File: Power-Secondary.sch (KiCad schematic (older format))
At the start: 50 parts, among them J1 Primary Battery +12VDC, J10 BPS +12V, J2 PRIM BATT DISCNCT, J3 BPS MAIN SUPPLY, J4 JUMP START, J5 DashBoard HORN CTL, J6 DashBoard DRV FAN CTL, J7 HORN +12V, J8 DRIVER FAN +12V, J9 RADIOS +12V, K1 G5Q-1, K2 G5Q-1, K3 G5Q-1, SW1 Batt Check, SW2 BPS PWR CHECK, SW3 RADIO PWR CHECK

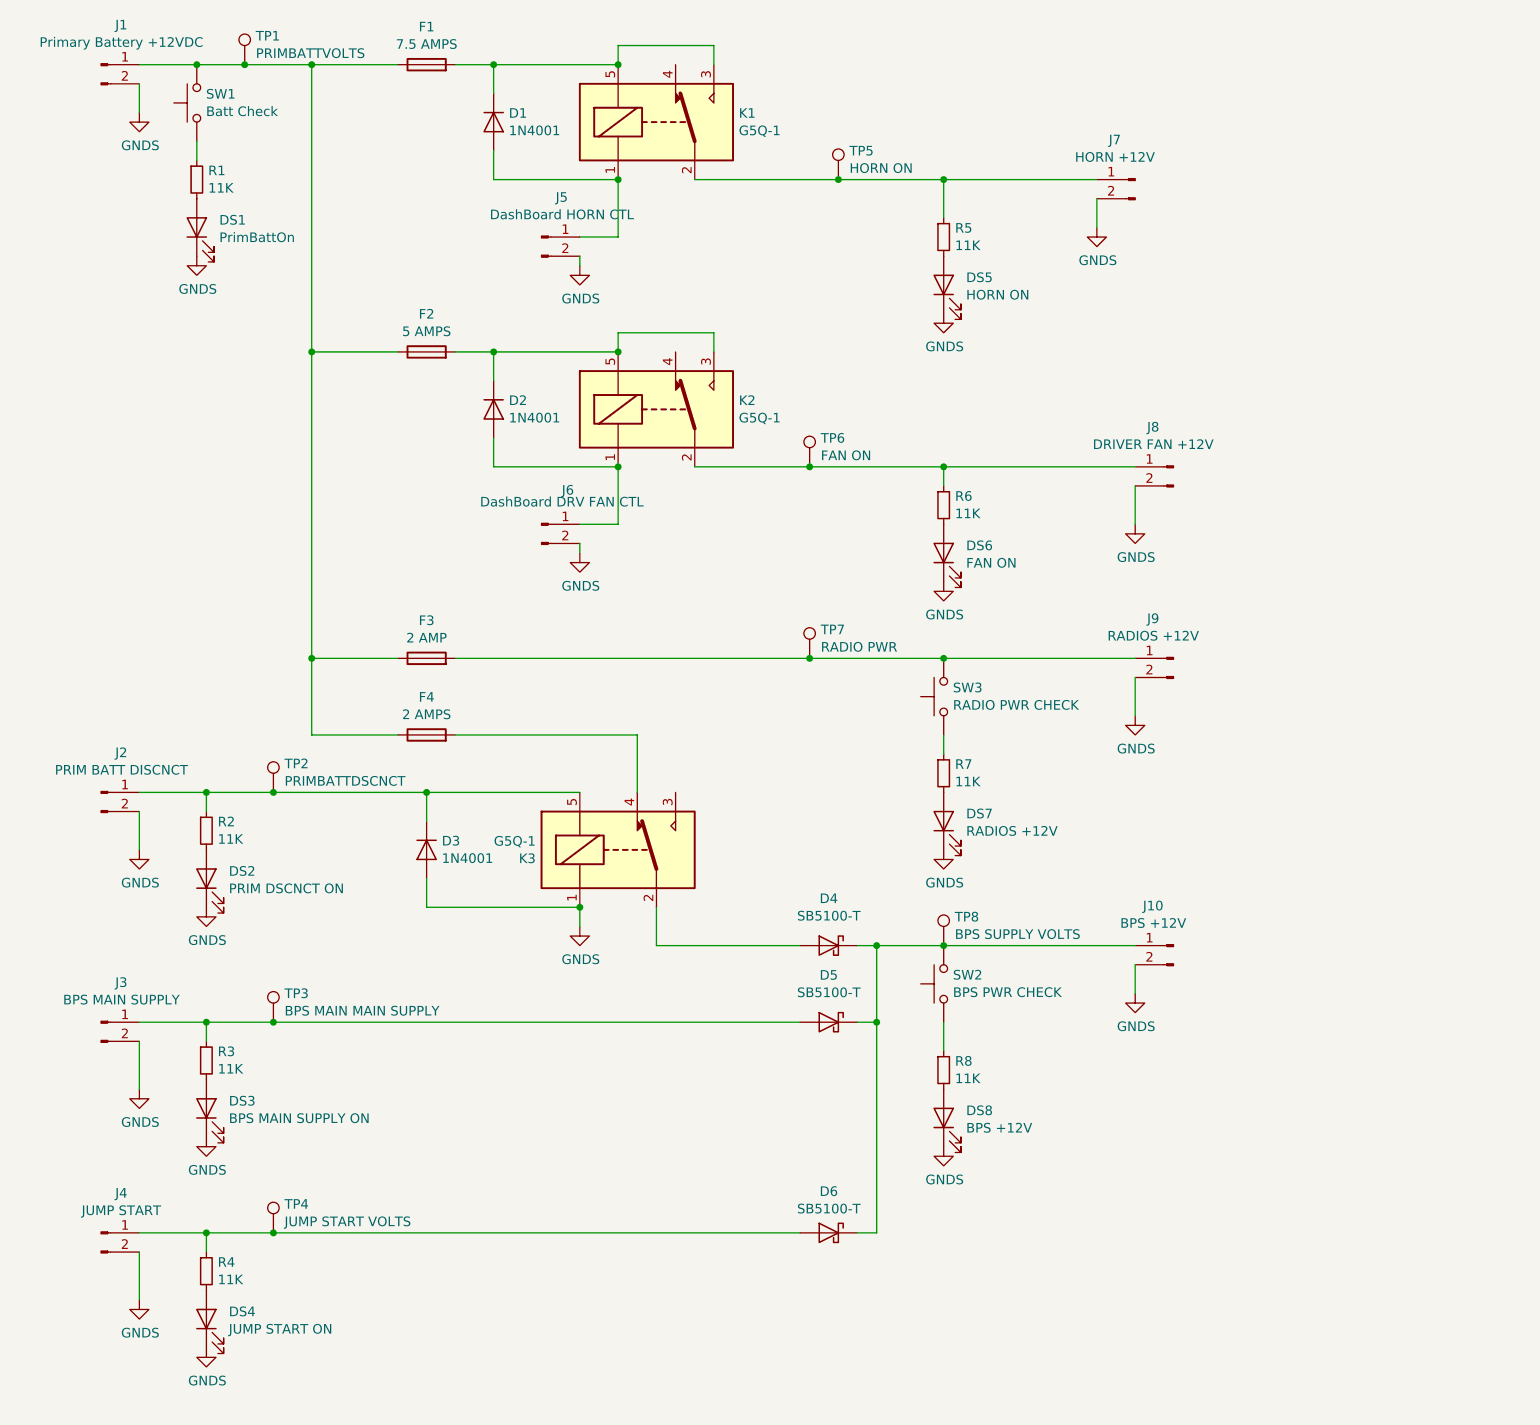
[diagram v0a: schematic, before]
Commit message: Secondary board v1.1 (#2)
* Updated PBB to better match Hannah's standards

* Adds power planes to secondary power board

* Updates schematics to match secondary power board v1.1

* Adds gitignore file

* Creates and deletes gerbers for release and finishes routing tracks

* Adds dimensions to PCB

Co-authored-by: Umar Burney <47867985+Emeraldness@users.noreply.github.com>
Co-authored-by: Sijin Woo <sijin.woo@utexas.edu>
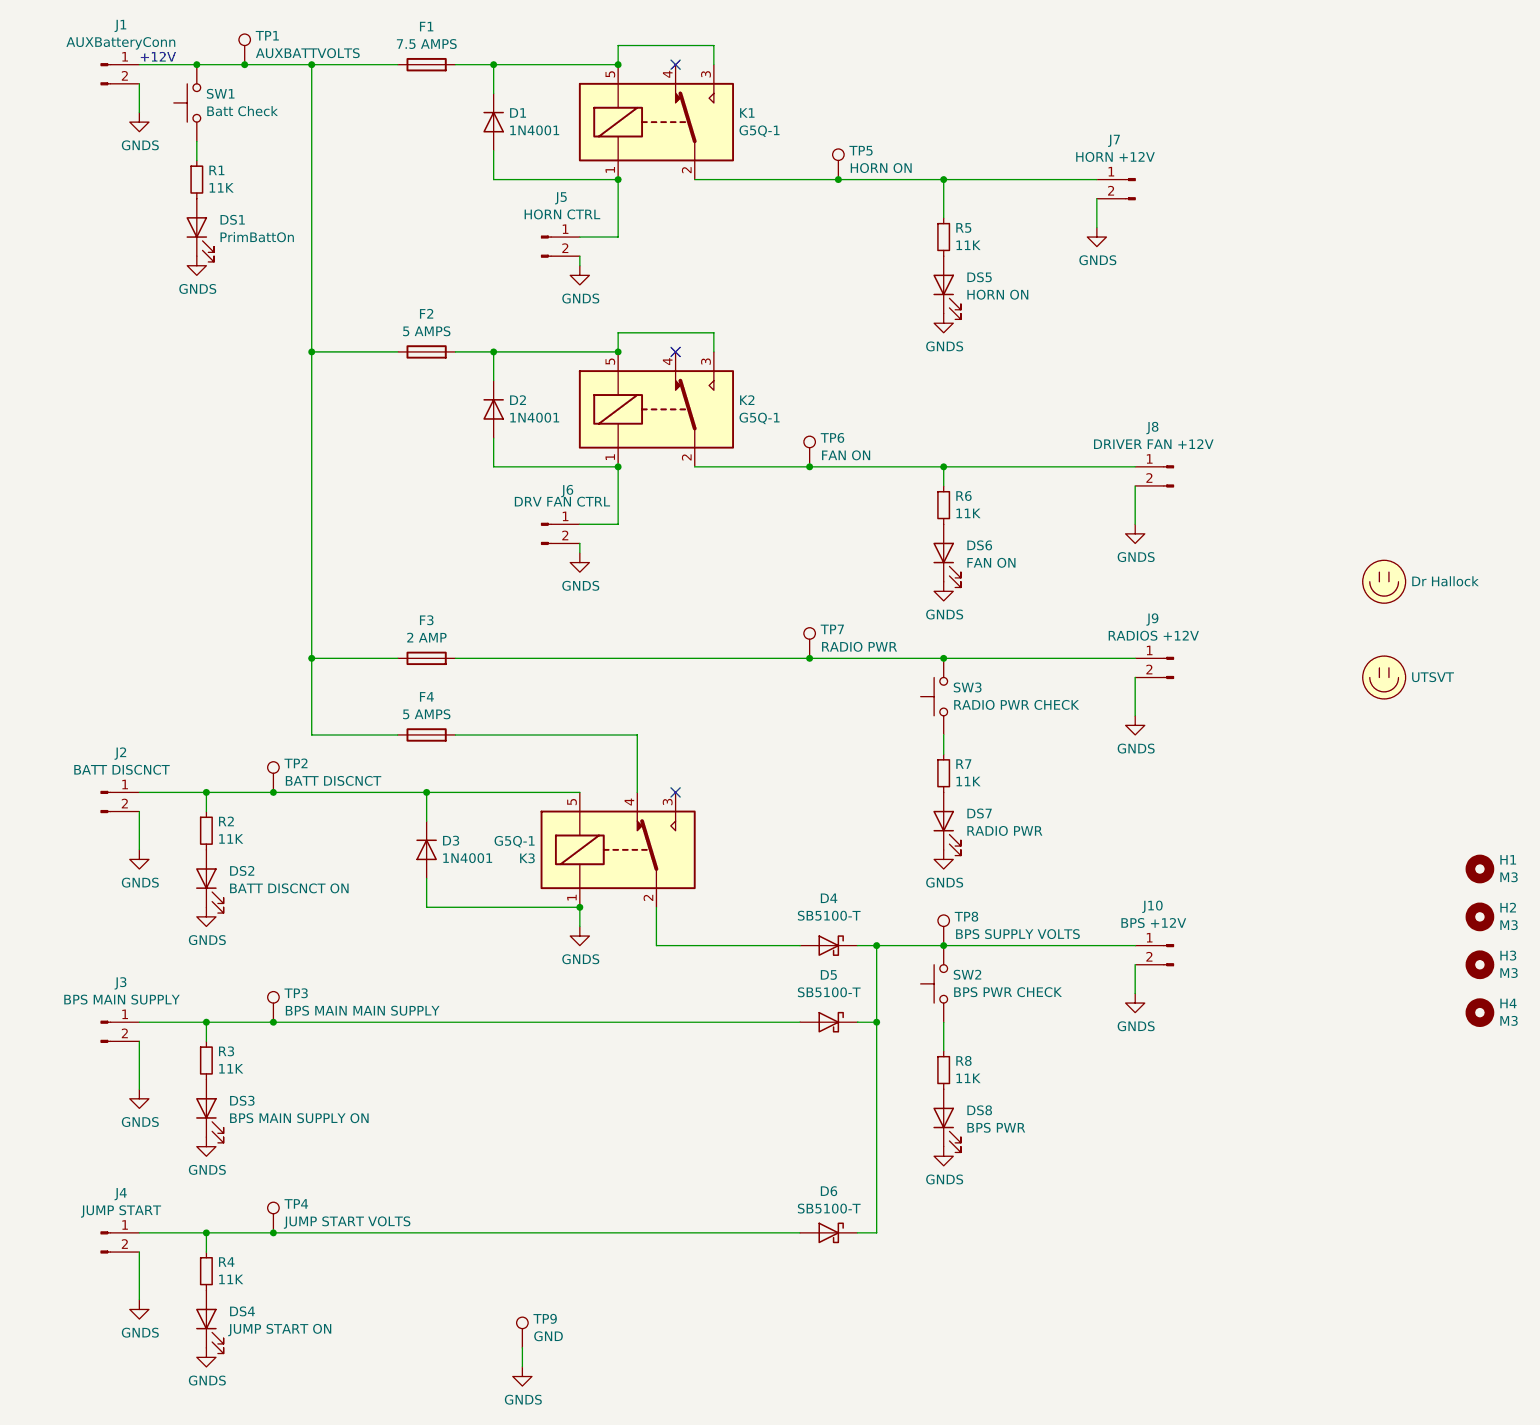
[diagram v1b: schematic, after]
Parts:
- added H1, H2, H3, H4: M3, MountingHole:MountingHole_3mm, symbol Mechanical:MountingHole
- added LOGO1: Dr Hallock, UTSVT_Special:Hallock_Image, symbol utsvt-misc:Logo_Placeholder
- added LOGO2: UTSVT, UTSVT_Special:UTSVT_Logo_Symbol, symbol utsvt-misc:Logo_Placeholder
- added TP9: GND, TestPoint:TestPoint_Pad_2.0x2.0mm, symbol Connector:TestPoint
- D1, D2, D3: footprint Diode_THT:D_DO-41_SOD81_P10.16mm_Horizontal -> Diode_THT:D_DO-15_P12.70mm_Horizontal
- D4, D5, D6: footprint Diode_THT:D_DO-201AD_P12.70mm_Horizontal -> Diode_THT:D_DO-201AD_P15.24mm_Horizontal
- DS2: value PRIM DSCNCT ON -> BATT DISCNCT ON
- DS7: value RADIOS +12V -> RADIO PWR
- DS8: value BPS +12V -> BPS PWR
- F4: value 2 AMPS -> 5 AMPS
- J1: value Primary Battery +12VDC -> AUXBatteryConn
- J2: value PRIM BATT DISCNCT -> BATT DISCNCT
- J5: value DashBoard HORN CTL -> HORN CTRL
- J6: value DashBoard DRV FAN CTL -> DRV FAN CTRL
- R1, R2, R3, R4, R5, R6, R7, R8: footprint Resistor_THT:R_Axial_DIN0204_L3.6mm_D1.6mm_P7.62mm_Horizontal -> Resistor_THT:R_Axial_DIN0207_L6.3mm_D2.5mm_P10.16mm_Horizontal
- TP1: value PRIMBATTVOLTS -> AUXBATTVOLTS
- TP2: value PRIMBATTDSCNCT -> BATT DISCNCT
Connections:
- net GNDS: now also TP9.1
- no-connect marks 0 -> 3
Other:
- note added: "+12V"

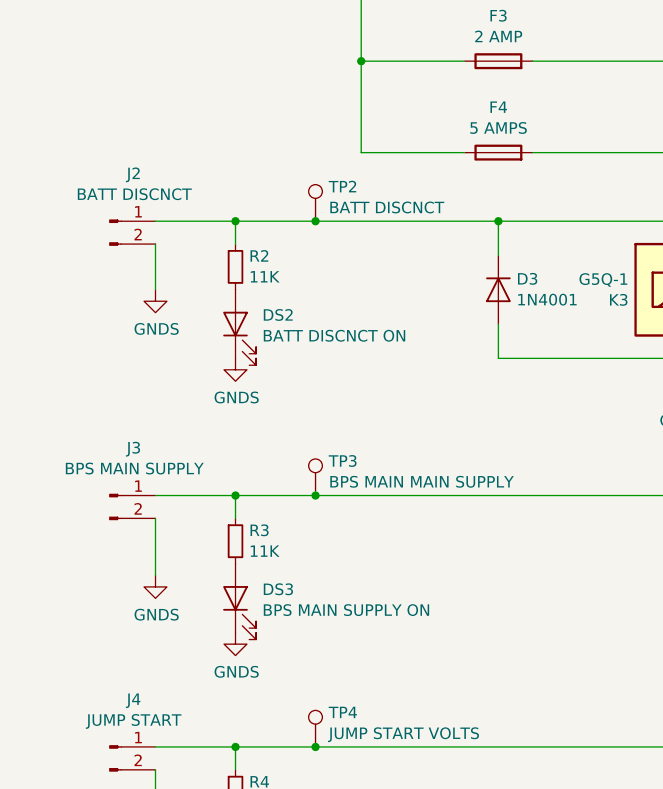
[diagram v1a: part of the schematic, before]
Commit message: Secondary Power Board CDR Edits (#3)
* Combines disconnect and main supply for BPS into one connector

* Rearranges labels and adds gerbers
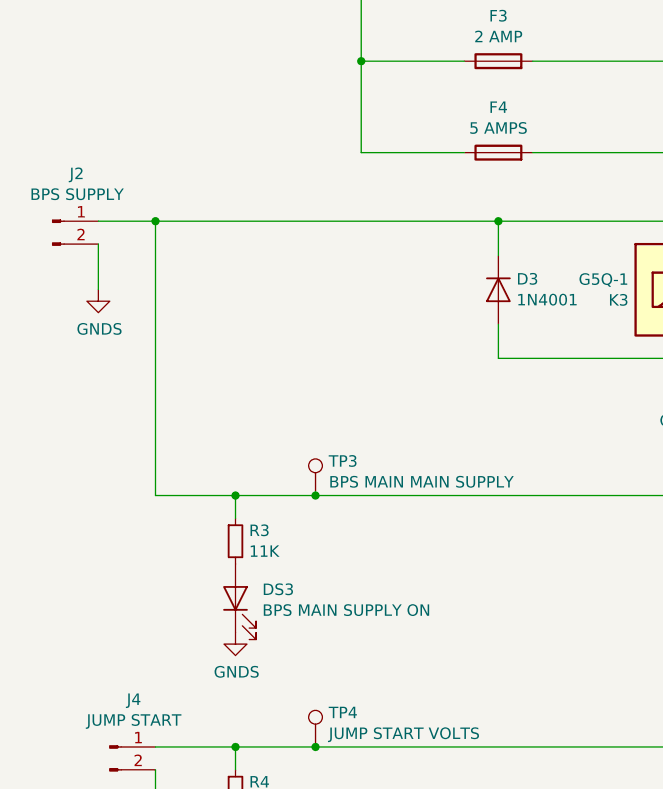
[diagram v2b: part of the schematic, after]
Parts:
- removed DS2: BATT DISCNCT ON, LED_THT:LED_D3.0mm, symbol Device:LED
- removed J3: BPS MAIN SUPPLY, Connector_Molex:Molex_Micro-Fit_3.0_43650-0215_1x02_P3.00mm_Vertical, symbol Connector:Conn_01x02_Male
- removed R2: 11K, Resistor_THT:R_Axial_DIN0207_L6.3mm_D2.5mm_P10.16mm_Horizontal, symbol Device:R_Small
- removed TP2: BATT DISCNCT, TestPoint:TestPoint_Pad_2.0x2.0mm, symbol Connector:TestPoint
- J2: value BATT DISCNCT -> BPS SUPPLY
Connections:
- net at D3.1 (K), J2.1 (Pin_1), K3.5: now also D5.2 (A), R3.1, TP3.1
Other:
- moved on the sheet: J2
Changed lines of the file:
@@
 L Connector:Conn_01x02_Male J2
 U 1 1 5BD1F5D8
-P 1800 4600
-F 0 "J2" H 1906 4778 50  0000 C BNN
-F 1 "BATT DISCNCT" H 1906 4687 50  0000 C BNN
-F 2 "Connector_Molex:Molex_Micro-Fit_3.0_43650-0215_1x02_P3.00mm_Vertical" H 1800 4600 50  0001 C CNN
-F 3 "~" H 1800 4600 50  0001 C CNN
-	1    1800 4600
+P 1550 4600
+F 0 "J2" H 1656 4778 50  0000 C BNN
+F 1 "BPS SUPPLY" H 1656 4687 50  0000 C BNN
+F 2 "Connector_Molex:Molex_Micro-Fit_3.0_43650-0215_1x02_P3.00mm_Vertical" H 1550 4600 50  0001 C CNN
+F 3 "~" H 1550 4600 50  0001 C CNN
+	1    1550 4600
 	1    0    0    -1
 $EndComp
@@
 L power:GNDS #PWR0109
 U 1 1 5BD2580C
-P 2000 4900
-F 0 "#PWR0109" H 2000 4650 50  0001 C CNN
-F 1 "GNDS" H 2005 4727 50  0000 C CNN
-F 2 "" H 2000 4900 50  0001 C CNN
-F 3 "" H 2000 4900 50  0001 C CNN
-	1    2000 4900
+P 1750 4900
+F 0 "#PWR0109" H 1750 4650 50  0001 C CNN
+F 1 "GNDS" H 1755 4727 50  0000 C CNN
+F 2 "" H 1750 4900 50  0001 C CNN
+F 3 "" H 1750 4900 50  0001 C CNN
+	1    1750 4900
 	1    0    0    -1
 $EndComp
@@
 $EndComp
 Wire Wire Line
-	2000 4600 2350 4600
-$Comp
-L power:GNDS #PWR0111
-U 1 1 5BD2B1A6
-P 2350 5200
-F 0 "#PWR0111" H 2350 4950 50  0001 C CNN
-F 1 "GNDS" H 2355 5027 50  0000 C CNN
-F 2 "" H 2350 5200 50  0001 C CNN
-F 3 "" H 2350 5200 50  0001 C CNN
-	1    2350 5200
-	1    0    0    -1
-$EndComp
-$Comp
-L Device:R_Small R2
-U 1 1 5BD2B1AC
-P 2350 4800
-F 0 "R2" H 2409 4846 50  0000 L CNN
-F 1 "11K" H 2409 4755 50  0000 L CNN
-F 2 "Resistor_THT:R_Axial_DIN0207_L6.3mm_D2.5mm_P10.16mm_Horizontal" H 2350 4800 50  0001 C CNN
-F 3 "~" H 2350 4800 50  0001 C CNN
-	1    2350 4800
-	1    0    0    -1
-$EndComp
-Wire Wire Line
-	2350 4700 2350 4600
-$Comp
-L Device:LED DS2
-U 1 1 5BD2B1B4
-P 2350 5050
-F 0 "DS2" V 2388 4933 50  0000 R CNN
-F 1 "BATT DISCNCT ON" V 2297 4933 50  0000 R CNN
-F 2 "LED_THT:LED_D3.0mm" H 2350 5050 50  0001 C CNN
-F 3 "~" H 2350 5050 50  0001 C CNN
-	1    2350 5050
-	0    -1   -1   0
-$EndComp
-Wire Wire Line
-	2000 4700 2000 4900
+	1750 4600 2000 4600
+Wire Wire Line
+	1750 4700 1750 4900
 $Comp
 L Device:Fuse F3
@@
 	0    -1   -1   0
 $EndComp
-Connection ~ 2350 4600
 Connection ~ 2900 800
 Wire Wire Line
@@
 Wire Wire Line
 	4600 4300 4600 4600
-Wire Wire Line
-	2350 4600 2700 4600
-$Comp
-L Connector:Conn_01x02_Male J3
-U 1 1 5BD7A592
-P 1800 5800
-F 0 "J3" H 1906 5978 50  0000 C BNN
-F 1 "BPS MAIN SUPPLY" H 1906 5887 50  0000 C BNN
-F 2 "Connector_Molex:Molex_Micro-Fit_3.0_43650-0215_1x02_P3.00mm_Vertical" H 1800 5800 50  0001 C CNN
-F 3 "~" H 1800 5800 50  0001 C CNN
-	1    1800 5800
-	1    0    0    -1
-$EndComp
-$Comp
-L power:GNDS #PWR0115
-U 1 1 5BD7A599
-P 2000 6150
-F 0 "#PWR0115" H 2000 5900 50  0001 C CNN
-F 1 "GNDS" H 2005 5977 50  0000 C CNN
-F 2 "" H 2000 6150 50  0001 C CNN
-F 3 "" H 2000 6150 50  0001 C CNN
-	1    2000 6150
-	1    0    0    -1
-$EndComp
-Wire Wire Line
-	2000 5900 2000 6150
-$Comp
-L power:GNDS #PWR0116
-U 1 1 5BD7A5A0
-P 2350 6400
-F 0 "#PWR0116" H 2350 6150 50  0001 C CNN
-F 1 "GNDS" H 2355 6227 50  0000 C CNN
-F 2 "" H 2350 6400 50  0001 C CNN
-F 3 "" H 2350 6400 50  0001 C CNN
-	1    2350 6400
-	1    0    0    -1
-$EndComp
-$Comp
-L Device:R_Small R3
-U 1 1 5BD7A5A6
-P 2350 6000
-F 0 "R3" H 2409 6046 50  0000 L CNN
-F 1 "11K" H 2409 5955 50  0000 L CNN
-F 2 "Resistor_THT:R_Axial_DIN0207_L6.3mm_D2.5mm_P10.16mm_Horizontal" H 2350 6000 50  0001 C CNN
-F 3 "~" H 2350 6000 50  0001 C CNN
-	1    2350 6000
-	1    0    0    -1
-$EndComp
-Wire Wire Line
-	2350 5900 2350 5800
-$Comp
-L Device:LED DS3
-U 1 1 5BD7A5AE
-P 2350 6250
-F 0 "DS3" V 2388 6133 50  0000 R CNN
-F 1 "BPS MAIN SUPPLY ON" V 2297 6133 50  0000 R CNN
-F 2 "LED_THT:LED_D3.0mm" H 2350 6250 50  0001 C CNN
-F 3 "~" H 2350 6250 50  0001 C CNN
-	1    2350 6250
-	0    -1   -1   0
-$EndComp
-Wire Wire Line
-	2000 5800 2350 5800
 $Comp
 L Connector:Conn_01x02_Male J10
@@
 Wire Wire Line
 	4300 5200 4300 5300
-Wire Wire Line
-	2350 5800 2700 5800
-Connection ~ 2350 5800
 Connection ~ 2350 6900
 $Comp
@@
 $EndComp
 $Comp
-L Connector:TestPoint TP2
-U 1 1 5BDF5BE5
-P 2700 4600
-F 0 "TP2" H 2758 4720 50  0000 L BNN
-F 1 "BATT DISCNCT" H 2758 4629 50  0000 L BNN
-F 2 "TestPoint:TestPoint_Pad_2.0x2.0mm" H 2900 4600 50  0001 C CNN
-F 3 "~" H 2900 4600 50  0001 C CNN
-	1    2700 4600
-	1    0    0    -1
-$EndComp
-$Comp
 L Connector:TestPoint TP3
 U 1 1 5BDF5C71
@@
 Wire Wire Line
 	2900 800  3350 800
-Connection ~ 2700 4600
 Connection ~ 2700 5800
 Wire Wire Line
@@
 Wire Wire Line
 	3850 2750 3850 2900
-Wire Wire Line
-	2700 4600 3500 4600
 $Comp
 L Diode:1N4001 D3
@@
 	1    0    0    -1
 $EndComp
+Wire Wire Line
+	2000 5800 2000 4600
+Connection ~ 2000 4600
+$Comp
+L Device:LED DS3
+U 1 1 5BD7A5AE
+P 2350 6250
+F 0 "DS3" V 2388 6133 50  0000 R CNN
+F 1 "BPS MAIN SUPPLY ON" V 2297 6133 50  0000 R CNN
+F 2 "LED_THT:LED_D3.0mm" H 2350 6250 50  0001 C CNN
+F 3 "~" H 2350 6250 50  0001 C CNN
+	1    2350 6250
+	0    -1   -1   0
+$EndComp
+Wire Wire Line
+	2350 5800 2700 5800
+Wire Wire Line
+	2000 5800 2350 5800
+Connection ~ 2350 5800
+Wire Wire Line
+	2350 5900 2350 5800
+$Comp
+L Device:R_Small R3
+U 1 1 5BD7A5A6
+P 2350 6000
+F 0 "R3" H 2409 6046 50  0000 L CNN
+F 1 "11K" H 2409 5955 50  0000 L CNN
+F 2 "Resistor_THT:R_Axial_DIN0207_L6.3mm_D2.5mm_P10.16mm_Horizontal" H 2350 6000 50  0001 C CNN
+F 3 "~" H 2350 6000 50  0001 C CNN
+	1    2350 6000
+	1    0    0    -1
+$EndComp
+$Comp
+L power:GNDS #PWR0116
+U 1 1 5BD7A5A0
+P 2350 6400
+F 0 "#PWR0116" H 2350 6150 50  0001 C CNN
+F 1 "GNDS" H 2355 6227 50  0000 C CNN
+F 2 "" H 2350 6400 50  0001 C CNN
+F 3 "" H 2350 6400 50  0001 C CNN
+	1    2350 6400
+	1    0    0    -1
+$EndComp
+Wire Wire Line
+	2000 4600 3500 4600
 $EndSCHEMATC
